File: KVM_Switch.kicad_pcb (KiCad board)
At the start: 4 copper layers, 100 x 70 mm, 118 parts, among them J1 HDMI_A, J2 HDMI_A, J3 HDMI_A, J4 USB_C_Receptacle_USB2.0_16P, J5 USB_C_Receptacle_USB2.0_16P, J6 USB_C_Receptacle_USB2.0_16P, J7 USB_A_Stacked, J8 USB_A_Stacked, SW1 SPST-NO, U1 TPD4E02B04DQA, U10 HD3SS215RTQR, U11 TLV75533PDBV, U12 STM32C031G6Ux, U13 USBLC6-2SC6, U14 TS3USB221AQRSERQ1, U15 USBLC6-2SC6, U16 USB2514B_Bi, U17 USBLC6-2SC6, U18 USBLC6-2SC6, U19 USBLC6-2SC6, U2 TPD4E02B04DQA, U20 USBLC6-2SC6, U3 TPD4E02B04DQA, U4 TPD4E02B04DQA, U5 TPD4E02B04DQA, U6 TPD4E02B04DQA, U7 TPD4E02B04DQA, U8 TPD4E02B04DQA, U9 TPD4E02B04DQA, X1 24MHz

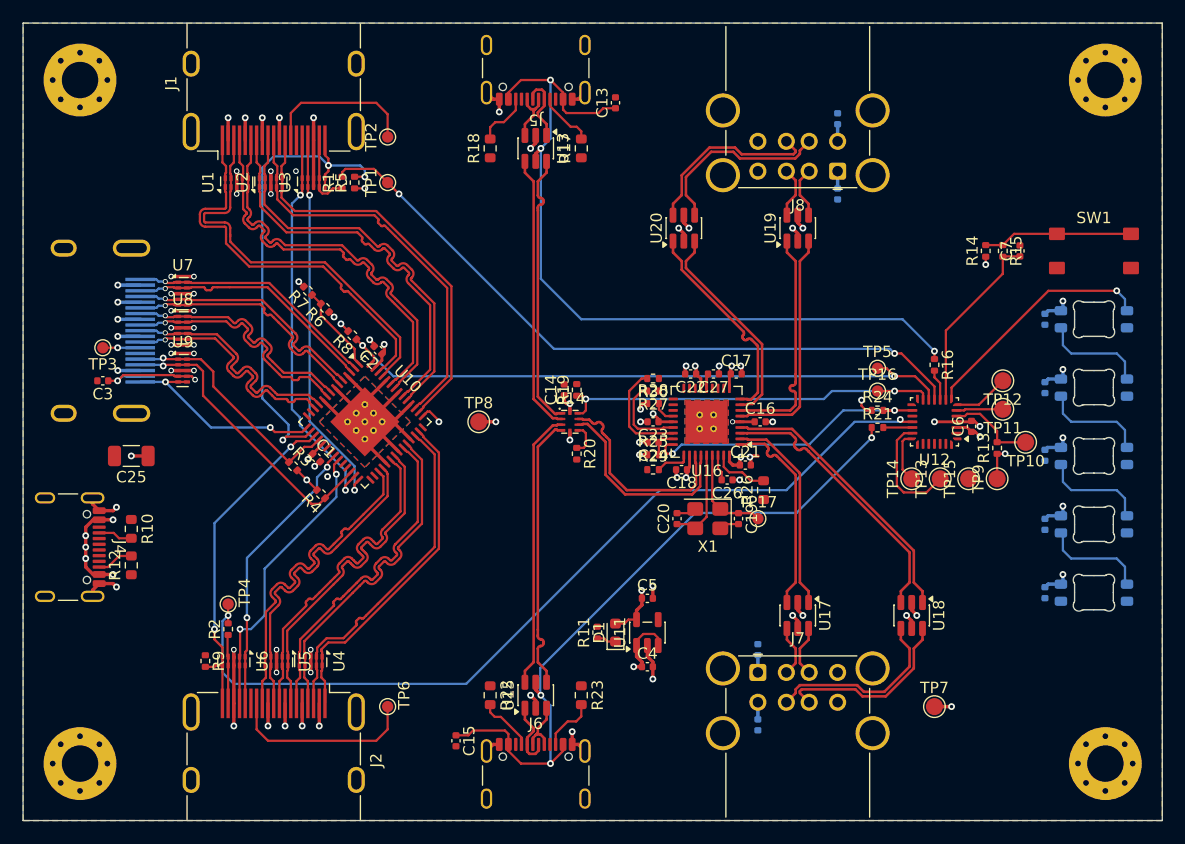
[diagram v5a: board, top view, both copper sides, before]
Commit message: USB fixes
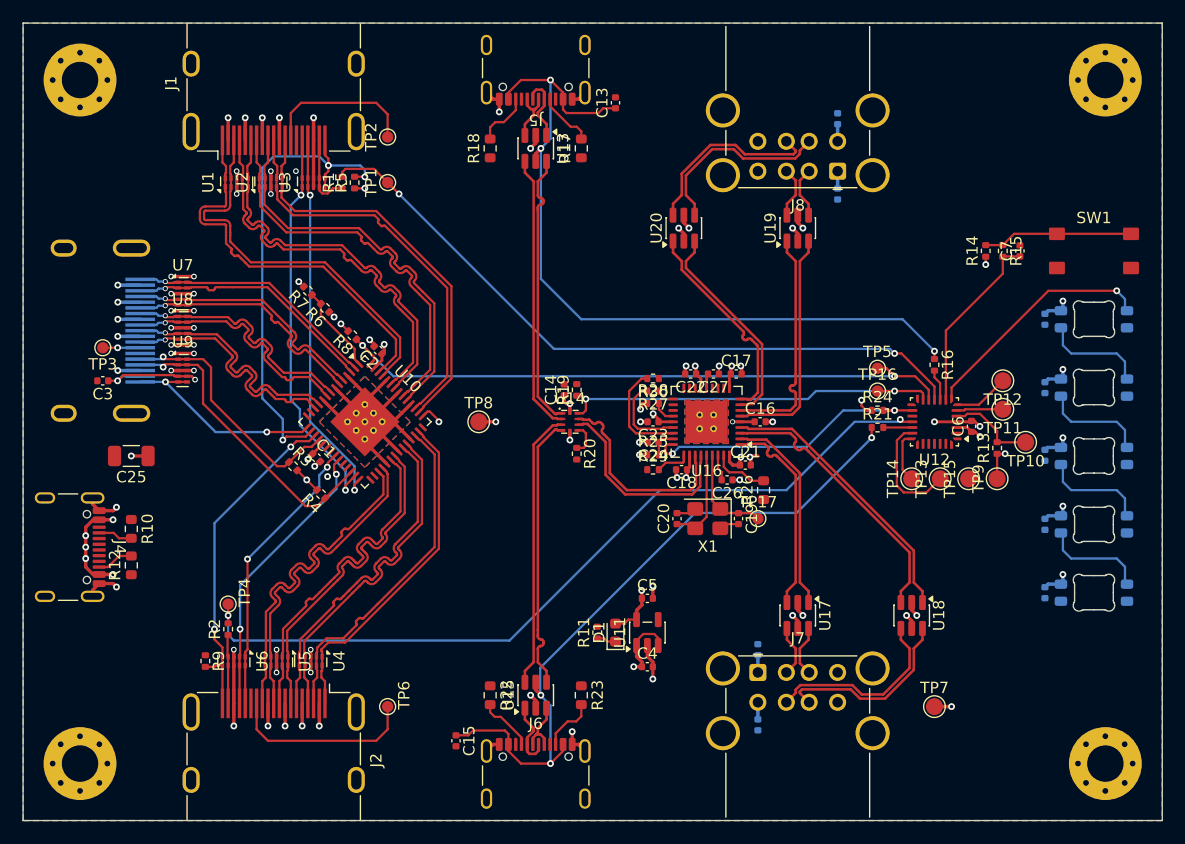
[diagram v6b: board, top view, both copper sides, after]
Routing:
- net /HDMI_Switch/DET_B: track 77.6 -> 71.8 mm
- net /HDMI_Switch/HDMI_OUT/SCL: track 21.1 -> 22.3 mm
- net /HDMI_Switch/HDMI_OUT/SDA: track 26.1 -> 26.9 mm
- net /HDMI_Switch/HDMI_IN_B/SDA: track 25.7 -> 25.2 mm

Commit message: Slikscreen cleanup
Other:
- board text added: "3V3"
- board text added: "CLK"
- board text added: "DIO"
- board text added: "GND"
- board text added: "RST"
- board text added: "RX"
- board text added: "TX"
